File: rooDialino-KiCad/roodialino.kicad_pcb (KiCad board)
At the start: 2 copper layers, 65 x 30 mm, 53 parts, among them J1 Raspi Connector, J2 ICSP, J3 FTDI, J4 IR Receiver, J5 IR LED, Q1 2N7002, Q2 2N7002, Q3 2N7002, SW1 SW_Push, U1 ATmega328P, U2 TSOP312xx, U3 TXS0108EPW, Y1 16 MHz

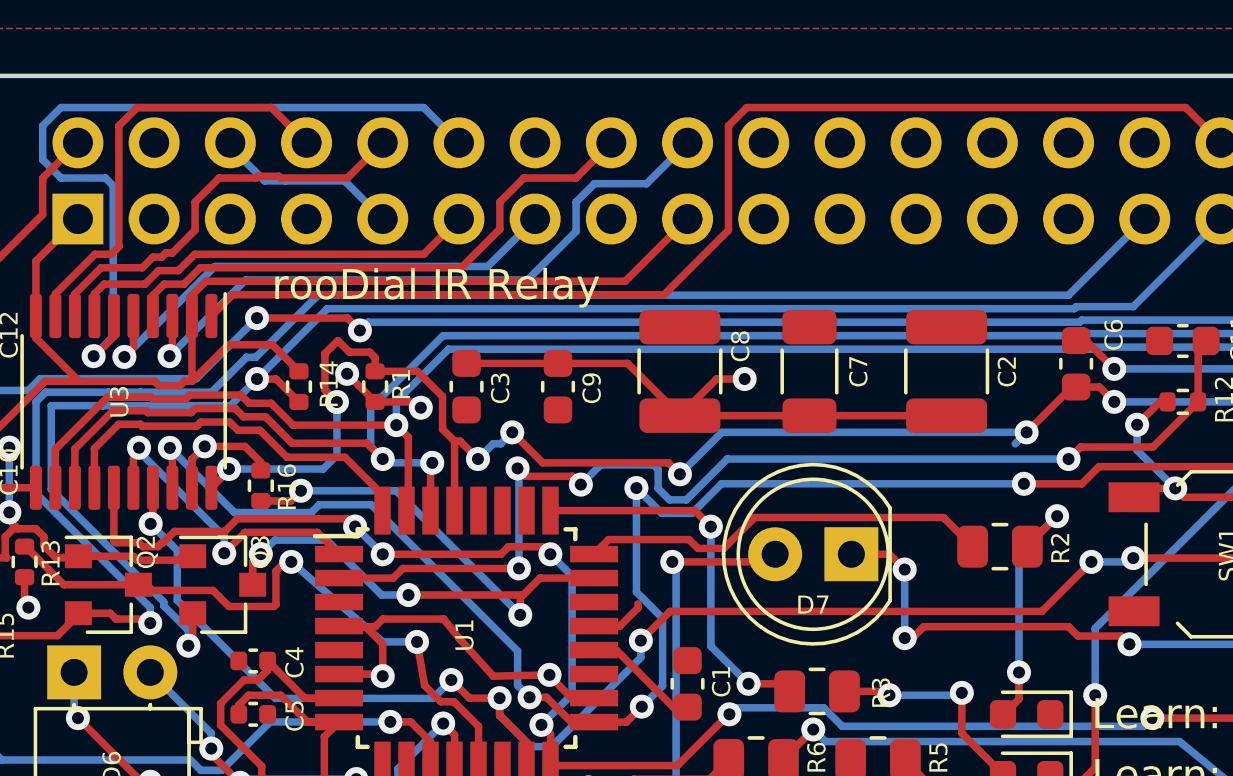
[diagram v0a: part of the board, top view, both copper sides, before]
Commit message: Better caps, less magic smoke!
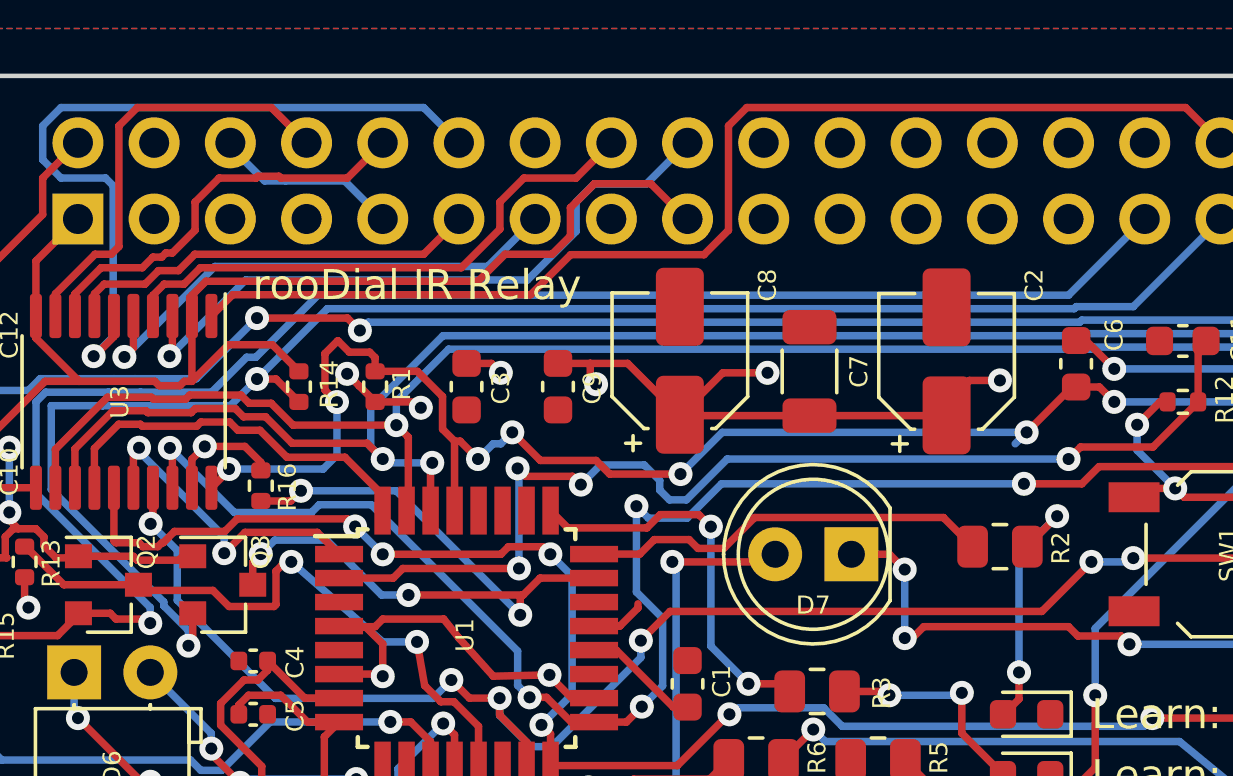
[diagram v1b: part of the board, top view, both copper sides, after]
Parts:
- C2: value 100u -> 47u; footprint Capacitor_SMD:C_1210_3225Metric -> Capacitor_SMD:CP_Elec_4x5.8
- C7: value 100u -> 47u
- C8: footprint Capacitor_SMD:C_1210_3225Metric -> Capacitor_SMD:CP_Elec_4x5.8
- moved C8 0.36 mm to (145.9, 100.6)
- moved C2 0.33 mm to (154.8, 100.6)
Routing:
- net +5V: track 58.0 -> 60.3 mm, vias 9 -> 12
- net +3V3: track 54.8 -> 56.3 mm
- net /SCK5: track 63.5 -> 62.8 mm

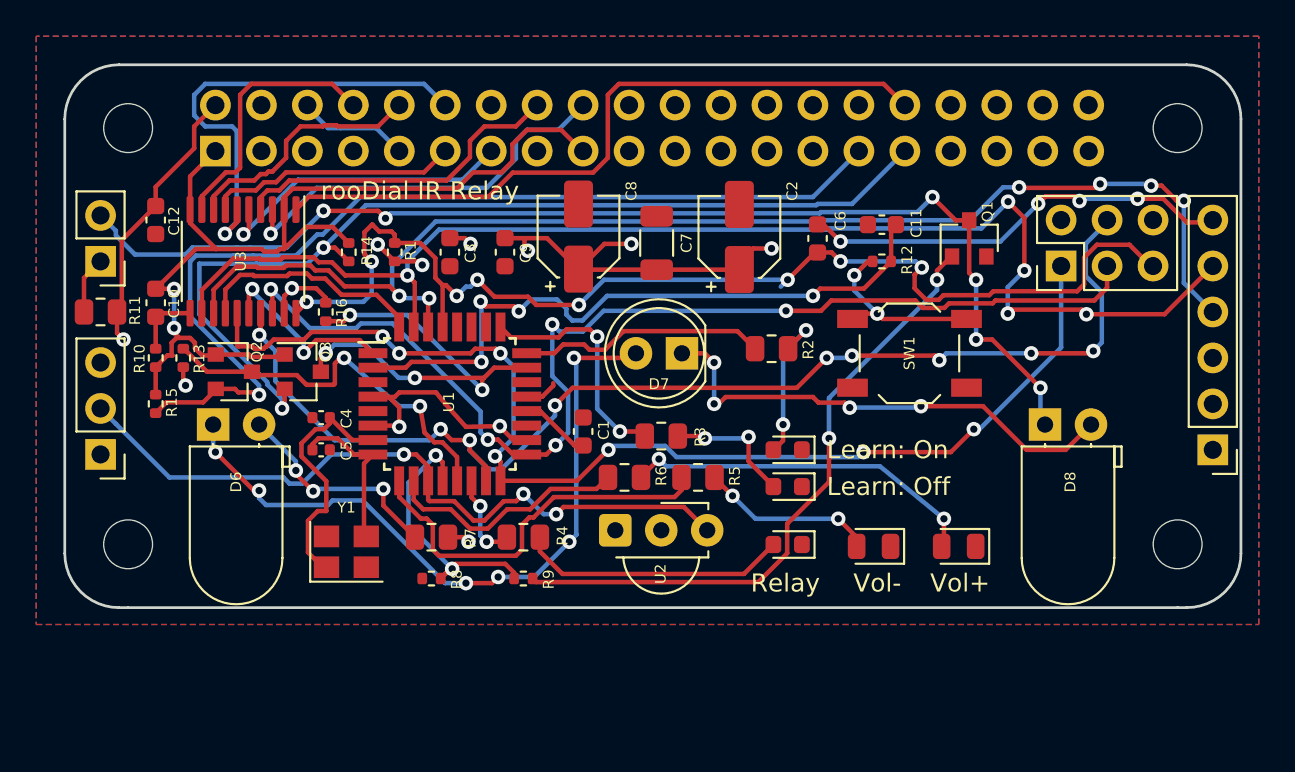
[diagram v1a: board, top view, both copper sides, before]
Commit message: Removing debounce RC
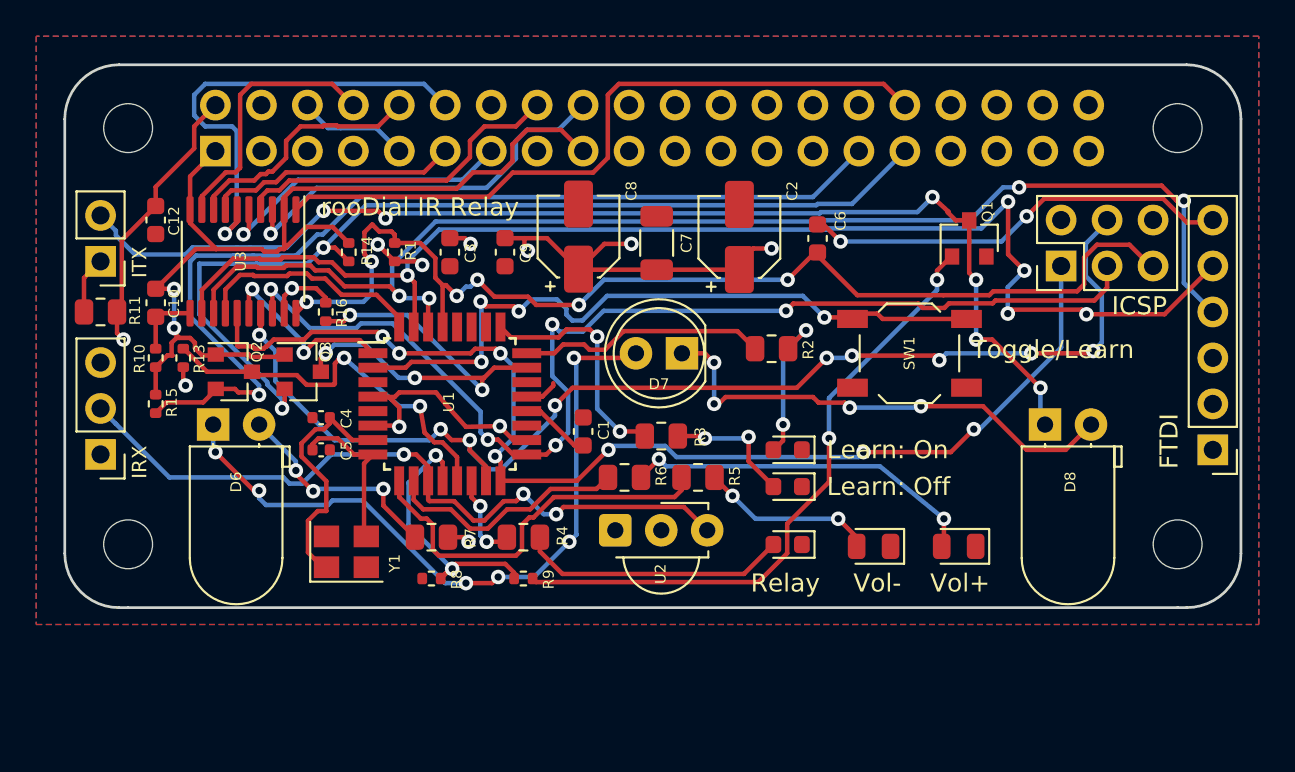
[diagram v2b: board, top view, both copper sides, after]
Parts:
- removed C11: 47n, Capacitor_SMD:C_0603_1608Metric
- removed R12: 10k, Resistor_SMD:R_0402_1005Metric
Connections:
- SW1 pad 2: Net-(R12-Pad1) -> /BTTN
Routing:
- net Net-(R12-Pad1): track 10.7 -> 0.00 mm, vias 2 -> 0
- net /BTTN: track 36.8 -> 39.0 mm
- net /~RST~: track 64.7 -> 62.7 mm, vias 8 -> 6
- net Net-(C6-Pad1): track 24.1 -> 23.9 mm, vias 4 -> 2
- net /RX5: track 71.1 -> 71.0 mm, vias 6 -> 4
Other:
- board text added: "5V"
- board text added: "FTDI"
- board text added: "GND"
- board text added: "ICSP"
- board text added: "IRX"
- board text added: "ITX"
- board text added: "JLCJLCJLCJLC"
- board text added: "RST"
- board text added: "RX"
- board text added: "TX"
- board text added: "Toggle/Learn"

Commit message: Tons of Trace Optimizations
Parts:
- moved R9 1.01 mm to (143.9, 119.5)
- moved R8 0.76 mm to (137.0, 119.5)
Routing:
- net /MISO3: track 26.0 -> 19.7 mm
- net GNDD: track 11.7 -> 17.0 mm
- net +3V3: track 56.3 -> 60.2 mm
- net /BTTN: track 39.0 -> 35.8 mm, vias 4 -> 2
- net +5V: track 60.3 -> 58.7 mm, vias 12 -> 14
- net /~RST~: track 62.7 -> 61.1 mm, vias 6 -> 4
- net Net-(Q1-Pad1): track 34.9 -> 33.8 mm
- net /D9: track 20.9 -> 22.0 mm
- net /VOL-3: track 17.1 -> 16.4 mm
- net /MOSI5: track 66.3 -> 65.6 mm
- net Net-(D8-Pad1): track 64.8 -> 64.3 mm
- net /TX5: track 71.8 -> 71.3 mm

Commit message: Levelshifter's OE gets permanently enabled. No need to ever have it low.
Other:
- board text added: "ICSP: use other side"
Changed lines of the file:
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@@
   (general
     (thickness 1.6)
-    (drawings 39)
+    (drawings 40)
     (tracks 809)
     (zones 0)
@@
     )
   )
+  (gr_text "ICSP: use \nother side" (at 171.069 100.838) (layer B.SilkS)
+    (effects (font (size 1 1) (thickness 0.15)) (justify left mirror))
+  )
   (gr_text Toggle/Learn (at 167.64 106.807) (layer F.SilkS)

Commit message: Saving before i size down some 0805s
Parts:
- added C11: 10u, Capacitor_Tantalum_SMD:CP_EIA-3216-18_Kemet-A, F.Cu at (151.0, 125.3)
- added JP1: SolderJumper_2_Open, Jumper:SolderJumper-2_P1.3mm_Open_RoundedPad1.0x1.5mm, B.Cu at (176.5, 107.3)
- added R12: 100, Resistor_SMD:R_0603_1608Metric, F.Cu at (142.7, 125.0)
- J4: value IR Receiver -> 2nd IRX
- U2: value TSOP312xx -> TSOP34838; footprint OptoDevice:Vishay_MINICAST-3Pin -> OptoDevice:Vishay_MOLD-3Pin
- moved U2 1.31 mm to (147.2, 117.9)
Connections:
- J3 pad 3: +5V -> Net-(J3-Pad3)
- J4 pad 1: GNDD -> /IRRCV
- J4 pad 2: /IRRCV -> GNDD
- J4 pad 3: +5V -> Net-(C11-Pad1)
- R10 pad 1: GNDD -> +3V3
- R10 pad 2: +3V3 -> Net-(R10-Pad2)
- U2 pad 1: GNDD -> /IRRCV
- U2 pad 2: +5V -> GNDD
- U2 pad 3: /IRRCV -> Net-(C11-Pad1)
- U3 pad 10: +3V3 -> Net-(R10-Pad2)
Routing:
- net /IRRCV: track 40.2 -> 31.2 mm
- net /MOSI5: track 65.6 -> 66.2 mm

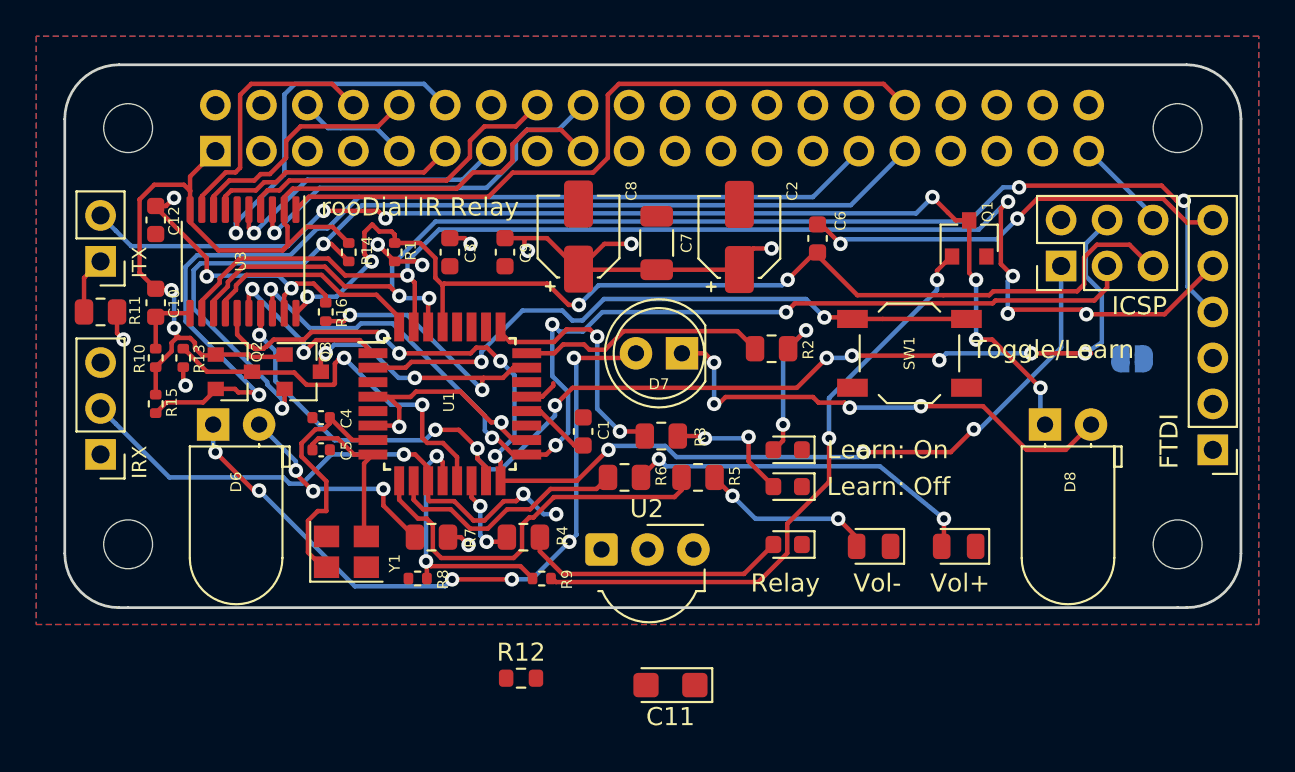
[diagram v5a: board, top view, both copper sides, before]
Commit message: Reroute to 0402 complete. Also, bugs fixed
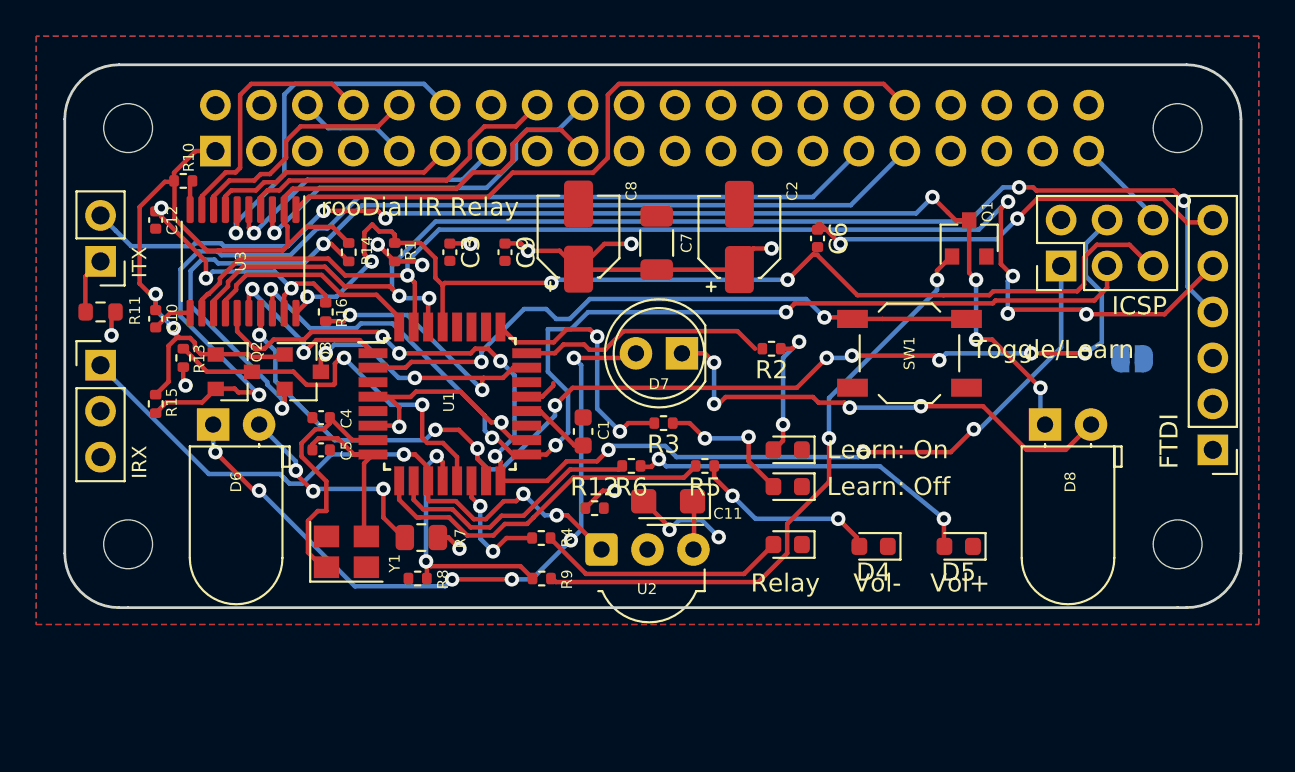
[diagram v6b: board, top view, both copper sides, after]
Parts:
- C10, C12, C3, C6, C9: footprint Capacitor_SMD:C_0603_1608Metric -> Capacitor_SMD:C_0402_1005Metric
- D4, D5: footprint LED_SMD:LED_0805_2012Metric -> LED_SMD:LED_0603_1608Metric
- R11: footprint Resistor_SMD:R_0805_2012Metric -> Resistor_SMD:R_0603_1608Metric
- R12: footprint Resistor_SMD:R_0603_1608Metric -> Resistor_SMD:R_0402_1005Metric
- R2, R3, R4, R5, R6: footprint Resistor_SMD:R_0805_2012Metric -> Resistor_SMD:R_0402_1005Metric
- moved R12 10.2 mm to (146.8, 115.6)
- moved C11 10.2 mm to (150.9, 115.2)
- moved R10 9.90 mm to (124.1, 97.5), turned to 0 degrees
- moved J4 4.93 mm to (119.5, 107.7), turned to 0 degrees
- moved R4 0.99 mm to (143.9, 117.2)
- moved C10 0.89 mm to (122.6, 105.1)
- moved R5 0.74 mm to (152.9, 113.2)
- moved R6 0.74 mm to (148.8, 113.2)
- moved R3 0.73 mm to (150.6, 110.9)
- moved R7 0.56 mm to (137.2, 117.2)
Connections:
- J4 pad 3: Net-(C11-Pad1) -> +5V
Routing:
- net /IRRCV: track 31.2 -> 35.6 mm
- net GNDD: track 17.0 -> 21.1 mm, vias 0 -> 2
- net Net-(C11-Pad1): track 0.00 -> 2.71 mm
- net /LEDVOL-: track 21.9 -> 19.8 mm
- net /LEDRSTATE: track 4.94 -> 6.85 mm
- net Net-(R10-Pad2): track 0.00 -> 1.68 mm
- net Net-(D3-Pad2): track 15.0 -> 13.8 mm
- net Net-(D1-Pad2): track 8.83 -> 7.72 mm
- net /LEDVOL+: track 13.6 -> 14.6 mm
- net /~RST~: track 61.1 -> 60.1 mm
- net +3V3: track 60.2 -> 60.9 mm
- net /MOSI5: track 66.2 -> 65.6 mm
- net Net-(D4-Pad2): track 9.74 -> 10.4 mm
- net /SCK5: track 62.2 -> 62.1 mm, vias 5 -> 4
- net +5V: track 58.7 -> 58.8 mm, vias 14 -> 15

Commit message: More bugfixes
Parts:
- moved JP1 0.11 mm to (176.4, 107.3)
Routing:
- net Net-(J3-Pad3): track 0.00 -> 3.76 mm
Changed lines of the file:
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@@
     (thickness 1.6)
     (drawings 40)
-    (tracks 811)
+    (tracks 812)
     (zones 0)
     (modules 54)
@@
   )
   (module Jumper:SolderJumper-2_P1.3mm_Open_RoundedPad1.0x1.5mm (layer B.Cu)
-    (at 176.515 107.315)
+    (at 176.403 107.3404)
     (descr "SMD Solder Jumper, 1x1.5mm, rounded Pads, 0.3mm gap, open")
     (tags "solder jumper open")
     (attr virtual)
-    (fp_text reference JP1 (at 0 1.8) (layer B.SilkS)
+    (fp_text reference JP1 (at 0 1.8) (layer B.SilkS) hide
       (effects (font (size 1 1) (thickness 0.15)) (justify mirror))
     )
@@
   (segment (start 152.305968 115.268968) (end 152.305968 117.823032) (width 0.25) (layer F.Cu) (net 70))
   (segment (start 152.305968 117.823032) (end 152.273 117.856) (width 0.25) (layer F.Cu) (net 70))
+  (segment (start 177.165 107.315) (end 180.9242 107.315) (width 0.25) (layer B.Cu) (net 71))
   (segment (start 124.457 99.0715) (end 124.457 97.6152) (width 0.25) (layer F.Cu) (net 72))
   (segment (start 124.457 97.6152) (end 124.6124 97.4598) (width 0.25) (layer F.Cu) (net 72))

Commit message: DRC complete
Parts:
- moved R12 8.34 mm to (154.9, 117.6), turned to 270 degrees
- moved D7 2.62 mm to (149.1, 106.5), turned to 0 degrees
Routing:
- net Net-(D6-Pad1): track 39.4 -> 47.0 mm, vias 6 -> 7
- net Net-(D7-Pad1): track 27.1 -> 31.3 mm, vias 4 -> 2
- net Net-(C11-Pad1): track 2.71 -> 5.99 mm
- net /LEDRON: track 13.8 -> 16.4 mm
- net GNDD: track 21.1 -> 20.2 mm
- net /LEDROFF: track 14.0 -> 13.4 mm
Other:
- board text added: "A"
- board text added: "K"
- board text added: "OUT"
- board text added: "Off-Codes"
- board text added: "On-Codes"
- board text added: "VCC"
- board text added: "rooControl IR Relay"
- board text removed: "FTDI"
- board text removed: "Learn: Off"
- board text removed: "Learn: On"
- board text removed: "Toggle/Learn"
- board text removed: "rooDial IR Relay"
